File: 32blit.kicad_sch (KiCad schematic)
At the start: 0 parts

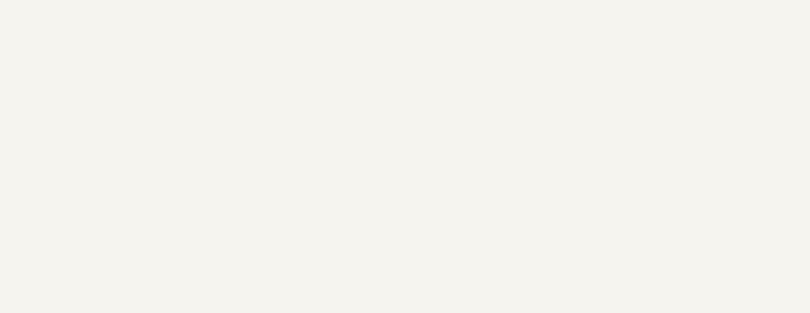
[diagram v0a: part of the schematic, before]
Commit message: Remove custom pimoroni frame
Makes the sch a bit hard to work with and recreating it in the .kicad_wks seems difficult
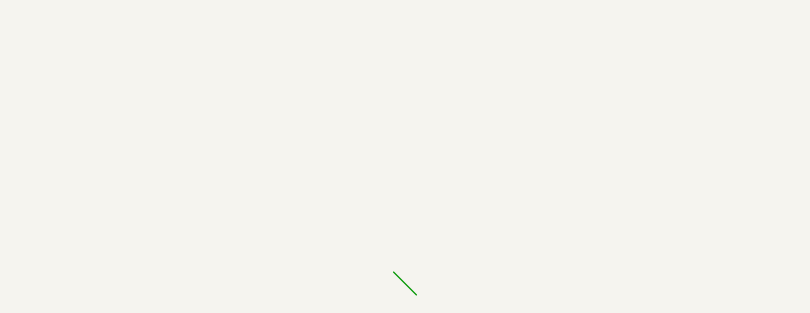
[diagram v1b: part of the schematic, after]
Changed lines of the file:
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@@
 (kicad_sch (version 20230121) (generator eeschema)
   (paper "A4")
+  (bus_entry (at 86.36 107.95) (size 2.54 2.54)
+    (stroke (width 0) (type default))
+  )
   (sheet (at 76.2 25.4) (size 12.7 3.81) (fields_autoplaced)
     (stroke (width 0) (type solid))

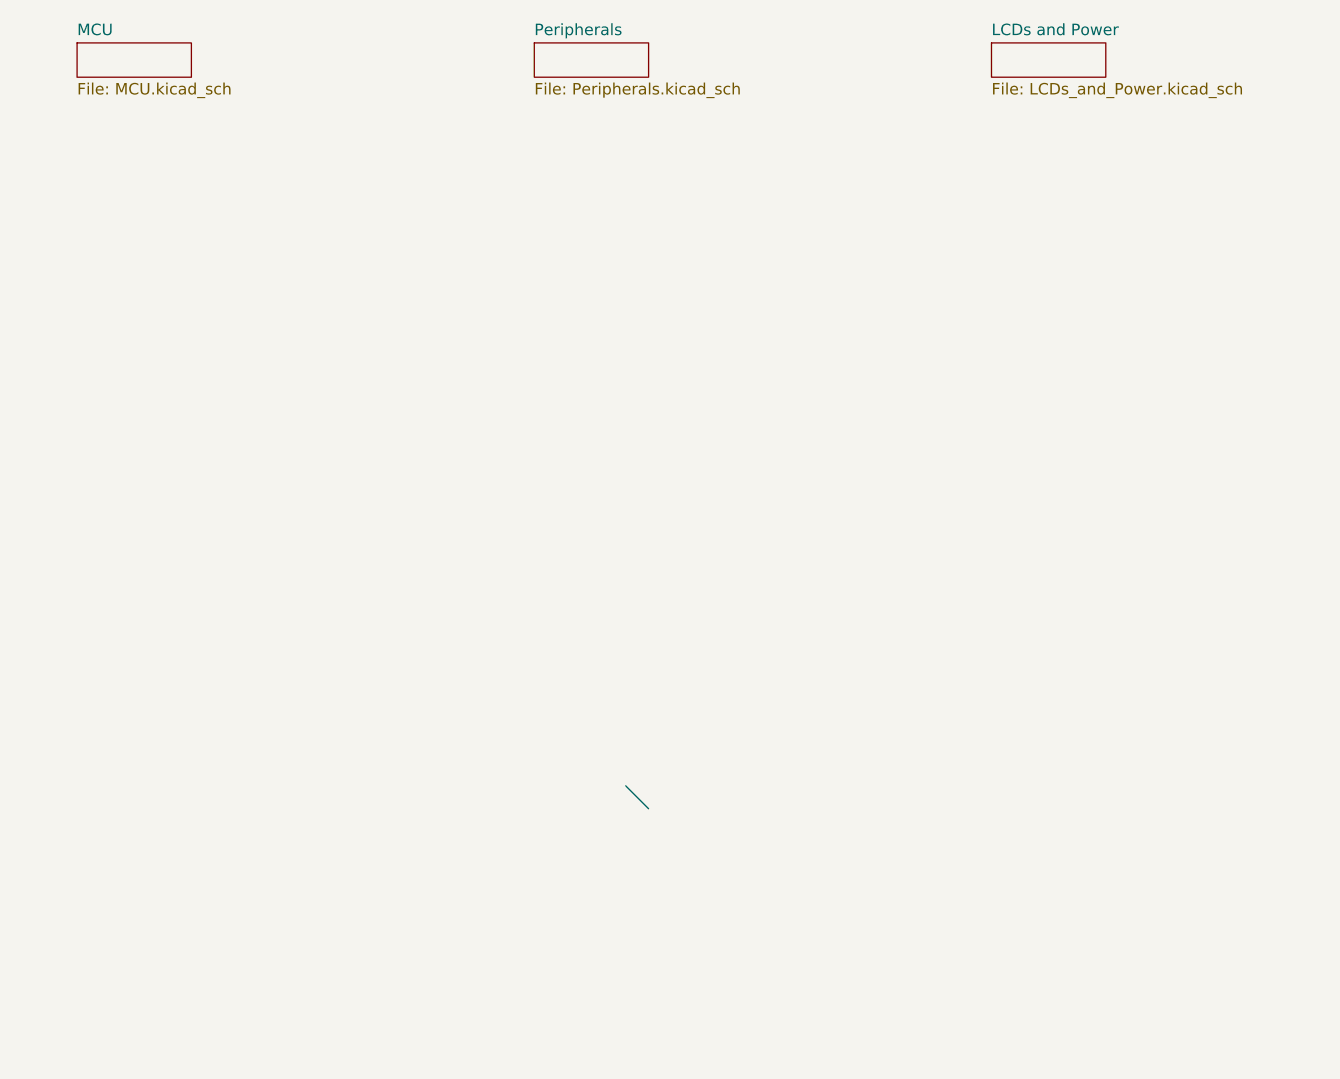
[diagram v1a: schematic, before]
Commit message: Giant schematic rework
Use as many kicad symbols as possiblem, adjust remaining imported symbols to make ERC happy and adjust some footprints for the new symbols
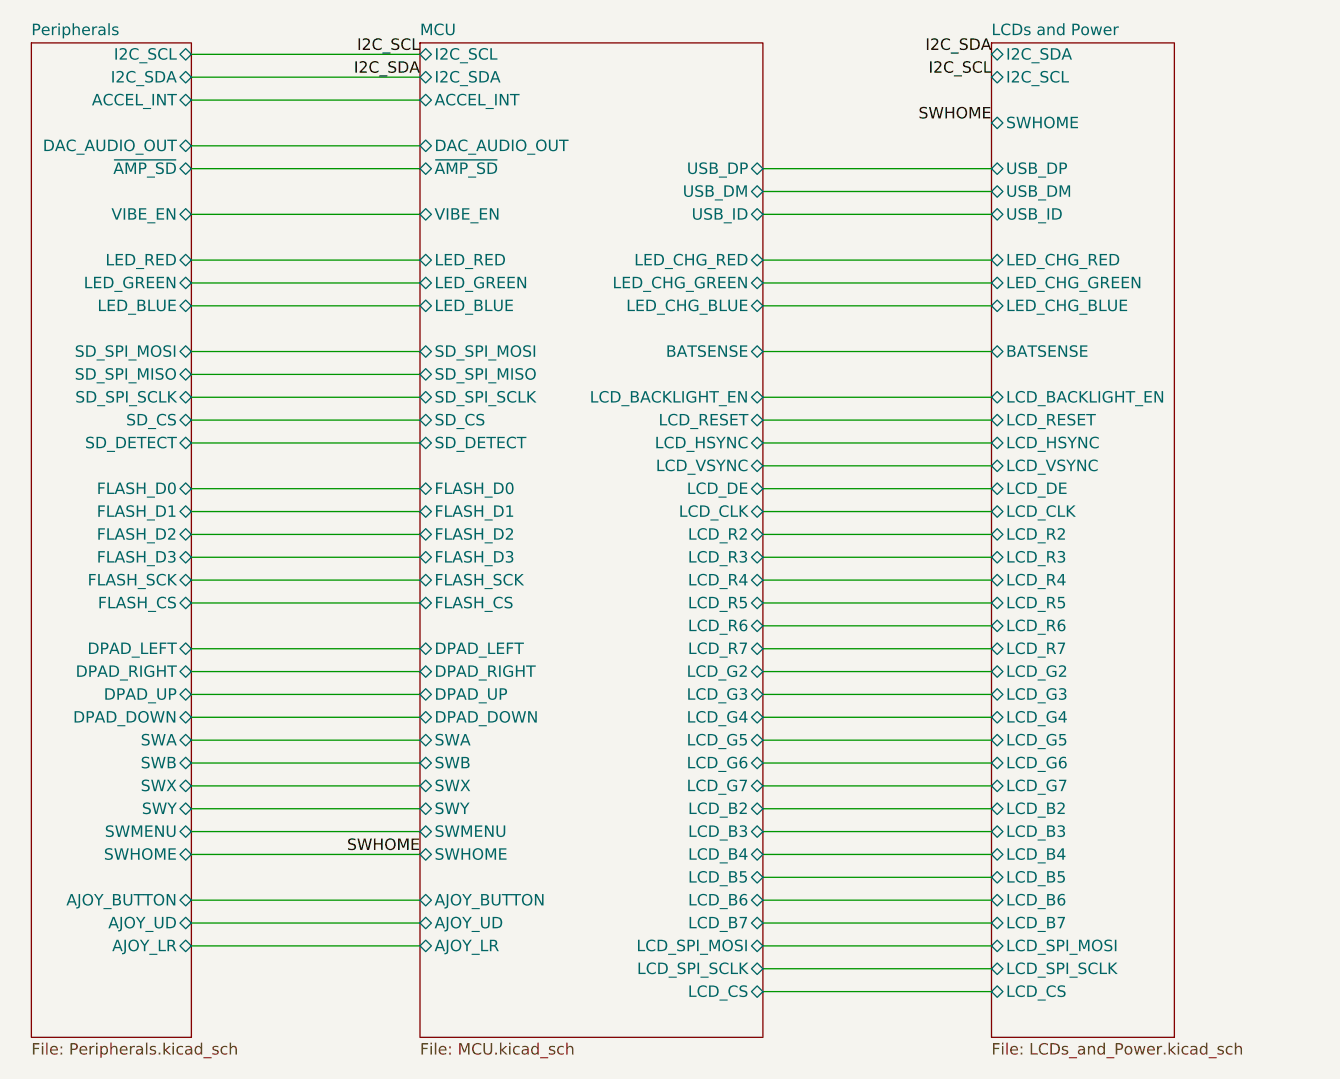
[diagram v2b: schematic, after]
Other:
- sheet LCDs and Power ports: added BATSENSE, I2C_SCL, I2C_SDA, LCD_B2, LCD_B3, LCD_B4, LCD_B5, LCD_B6, LCD_B7, LCD_BACKLIGHT_EN, LCD_CLK, LCD_CS, LCD_DE, LCD_G2, LCD_G3, LCD_G4, LCD_G5, LCD_G6, LCD_G7, LCD_HSYNC, LCD_R2, LCD_R3, LCD_R4, LCD_R5, LCD_R6, LCD_R7, LCD_RESET, LCD_SPI_MOSI, LCD_SPI_SCLK, LCD_VSYNC, LED_CHG_BLUE, LED_CHG_GREEN, LED_CHG_RED, SWHOME, USB_DM, USB_DP, USB_ID; removed none
- sheet MCU ports: added ACCEL_INT, AJOY_BUTTON, AJOY_LR, AJOY_UD, BATSENSE, DAC_AUDIO_OUT, DPAD_DOWN, DPAD_LEFT, DPAD_RIGHT, DPAD_UP, FLASH_CS, FLASH_D0, FLASH_D1, FLASH_D2, FLASH_D3, FLASH_SCK, I2C_SCL, I2C_SDA, LCD_B2, LCD_B3, LCD_B4, LCD_B5, LCD_B6, LCD_B7, LCD_BACKLIGHT_EN, LCD_CLK, LCD_CS, LCD_DE, LCD_G2, LCD_G3, LCD_G4, LCD_G5, LCD_G6, LCD_G7, LCD_HSYNC, LCD_R2, LCD_R3, LCD_R4, LCD_R5, LCD_R6, LCD_R7, LCD_RESET, LCD_SPI_MOSI, LCD_SPI_SCLK, LCD_VSYNC, LED_BLUE, LED_CHG_BLUE, LED_CHG_GREEN, LED_CHG_RED, LED_GREEN, LED_RED, SD_CS, SD_DETECT, SD_SPI_MISO, SD_SPI_MOSI, SD_SPI_SCLK, SWA, SWB, SWHOME, SWMENU, SWX, SWY, USB_DM, USB_DP, USB_ID, VIBE_EN, ~{AMP_SD}; removed none
- sheet Peripherals ports: added ACCEL_INT, AJOY_BUTTON, AJOY_LR, AJOY_UD, DAC_AUDIO_OUT, DPAD_DOWN, DPAD_LEFT, DPAD_RIGHT, DPAD_UP, FLASH_CS, FLASH_D0, FLASH_D1, FLASH_D2, FLASH_D3, FLASH_SCK, I2C_SCL, I2C_SDA, LED_BLUE, LED_GREEN, LED_RED, SD_CS, SD_DETECT, SD_SPI_MISO, SD_SPI_MOSI, SD_SPI_SCLK, SWA, SWB, SWHOME, SWMENU, SWX, SWY, VIBE_EN, ~{AMP_SD}; removed none
